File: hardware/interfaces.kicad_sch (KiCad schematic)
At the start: 13 parts, among them J10 REC LED, J4 LCD, J5 MIC 3V3, J6 AMP 5V, J8 PTT, J9 PAGE

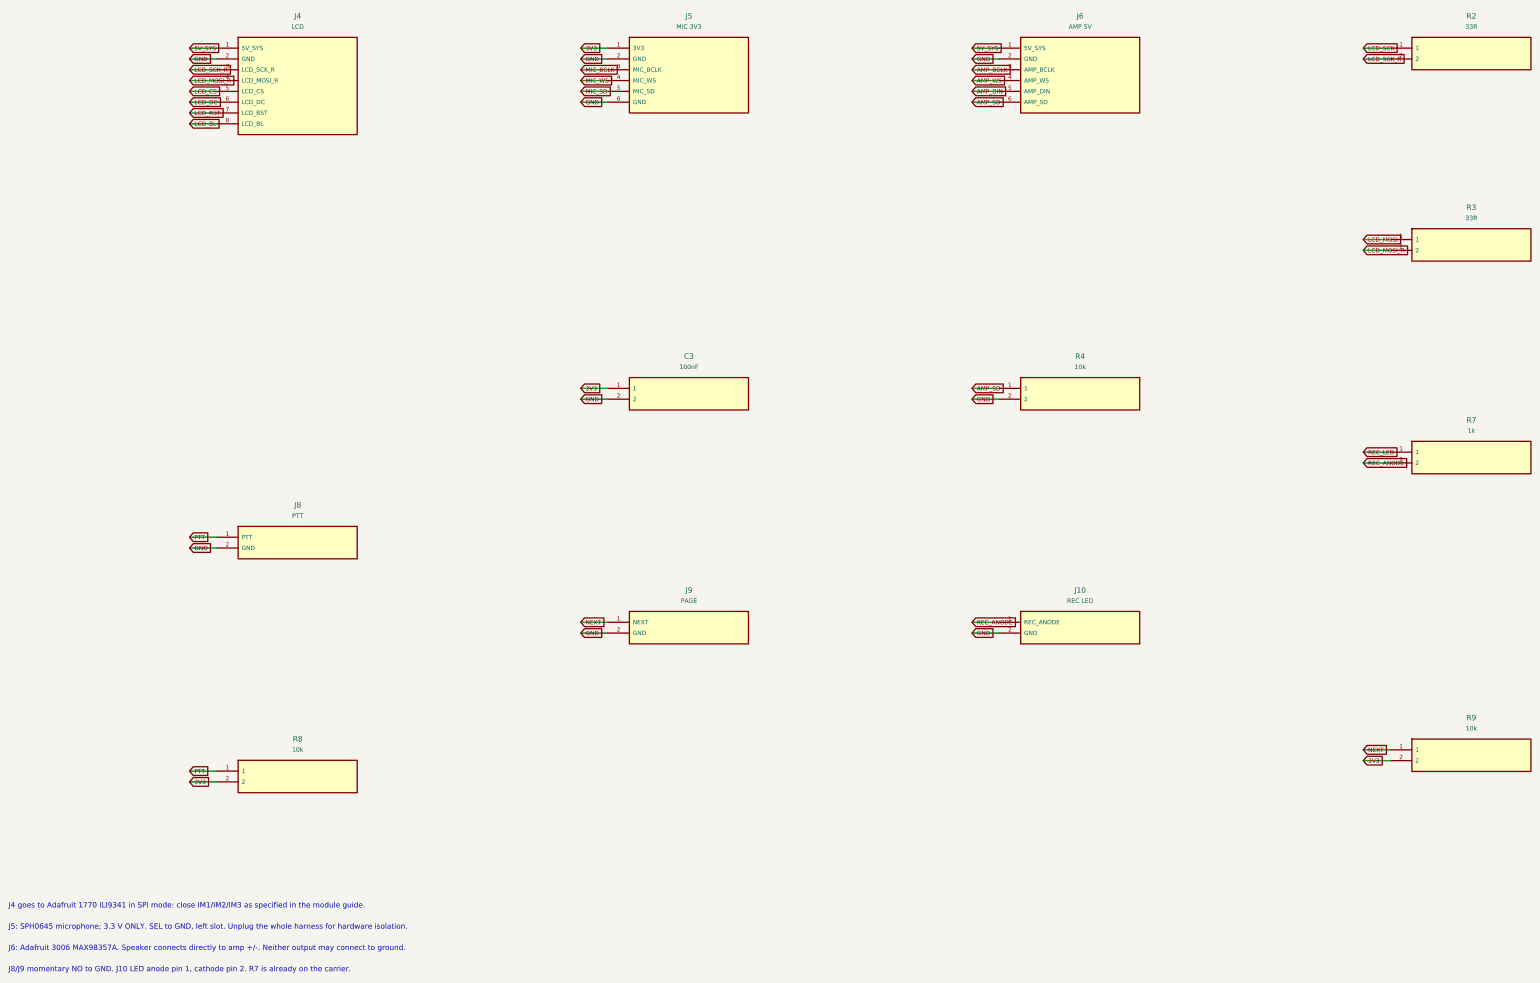
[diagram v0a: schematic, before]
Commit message: engineering: Rev B zero-interference CAD, sealed STL meshes and carrier corrections
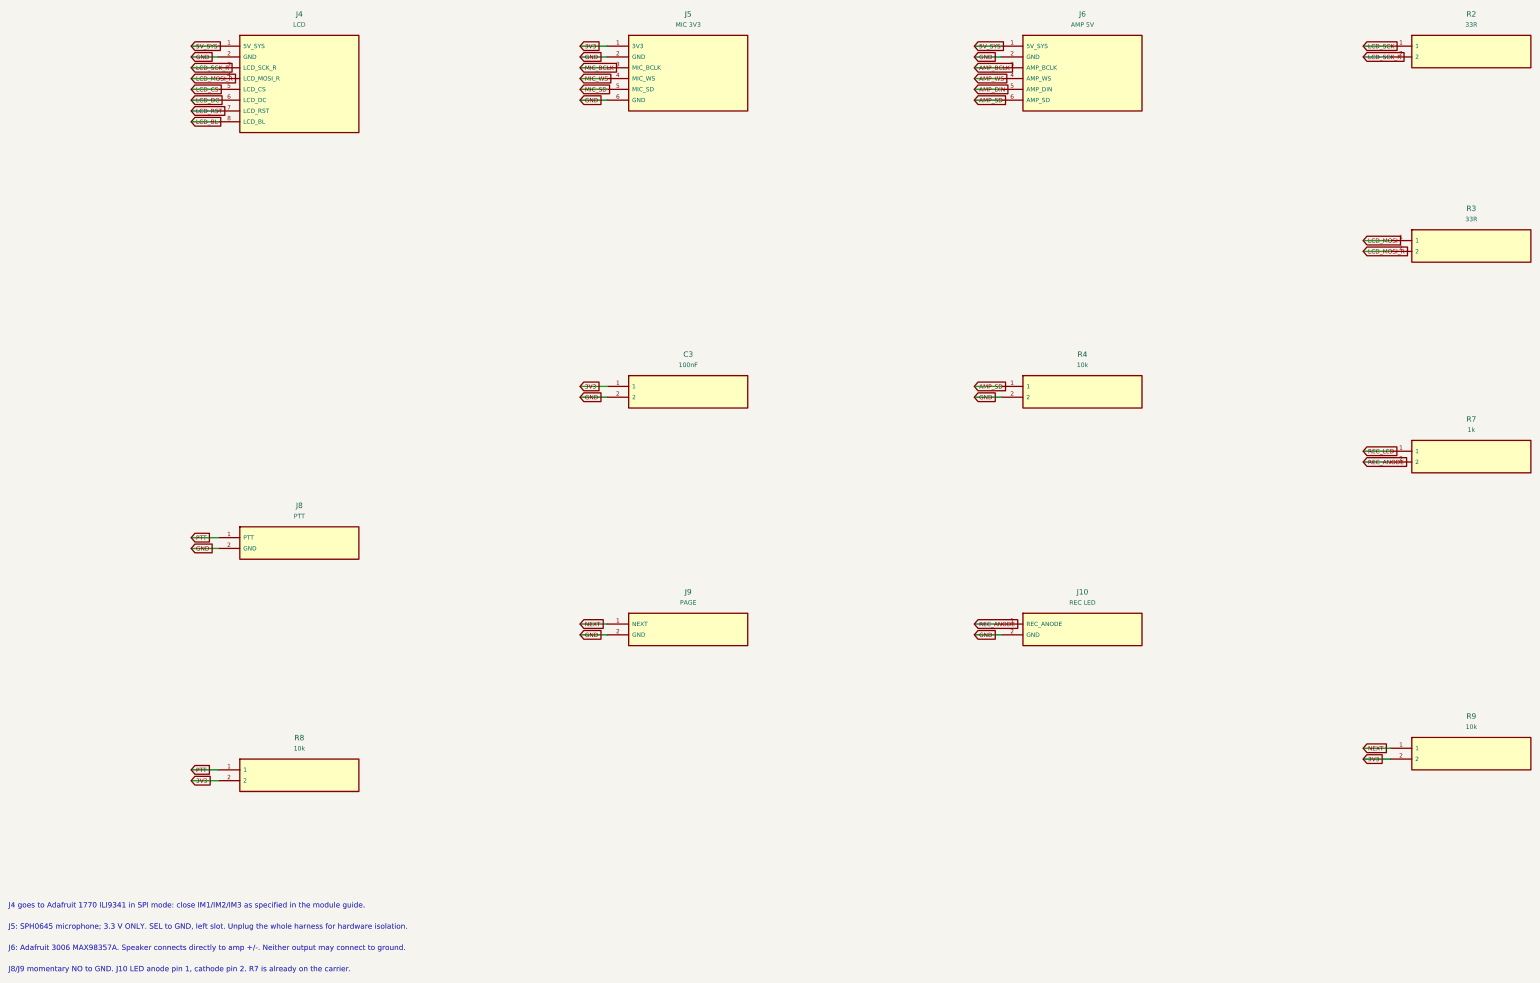
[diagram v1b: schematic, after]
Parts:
- C3: footprint Aether:C_0805_2012Metric -> Aether:C_0805_2012Metric_C3
- J10: footprint Aether:XH_1x02_P2.50 -> Aether:XH_1x02_P2.50_J10
- J4: footprint Aether:XH_1x08_P2.50 -> Aether:XH_1x08_P2.50_J4
- J5: footprint Aether:XH_1x06_P2.50 -> Aether:XH_1x06_P2.50_J5
- J6: footprint Aether:XH_1x06_P2.50 -> Aether:XH_1x06_P2.50_J6
- J8: footprint Aether:XH_1x02_P2.50 -> Aether:XH_1x02_P2.50_J8
- J9: footprint Aether:XH_1x02_P2.50 -> Aether:XH_1x02_P2.50_J9
- R2: footprint Aether:R_0805_2012Metric -> Aether:R_0805_2012Metric_R2
- R3: footprint Aether:R_0805_2012Metric -> Aether:R_0805_2012Metric_R3
- R4: footprint Aether:R_0805_2012Metric -> Aether:R_0805_2012Metric_R4
- R7: footprint Aether:R_0805_2012Metric -> Aether:R_0805_2012Metric_R7
- R8: footprint Aether:R_0805_2012Metric -> Aether:R_0805_2012Metric_R8
- R9: footprint Aether:R_0805_2012Metric -> Aether:R_0805_2012Metric_R9
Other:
- moved on the sheet: J10, J4, J6, R4
